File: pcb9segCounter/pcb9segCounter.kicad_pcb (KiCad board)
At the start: 2 copper layers, 72.2 x 78.5 mm, 52 parts, among them J1 SAO, J2 AVR-ISP-6, U1 ATtiny84A-SS

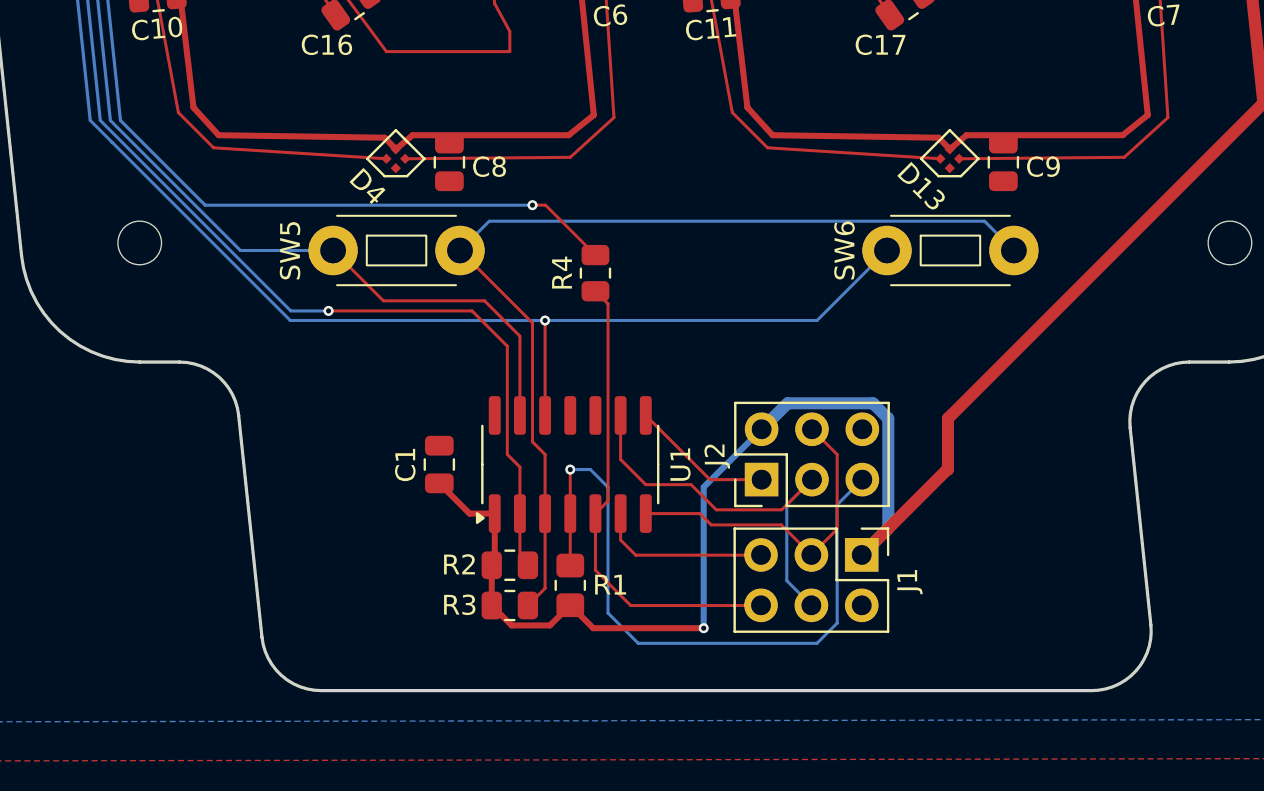
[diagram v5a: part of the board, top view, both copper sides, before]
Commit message: adding 3d model which was used to generate board outline, commiting before adding i2c pullups
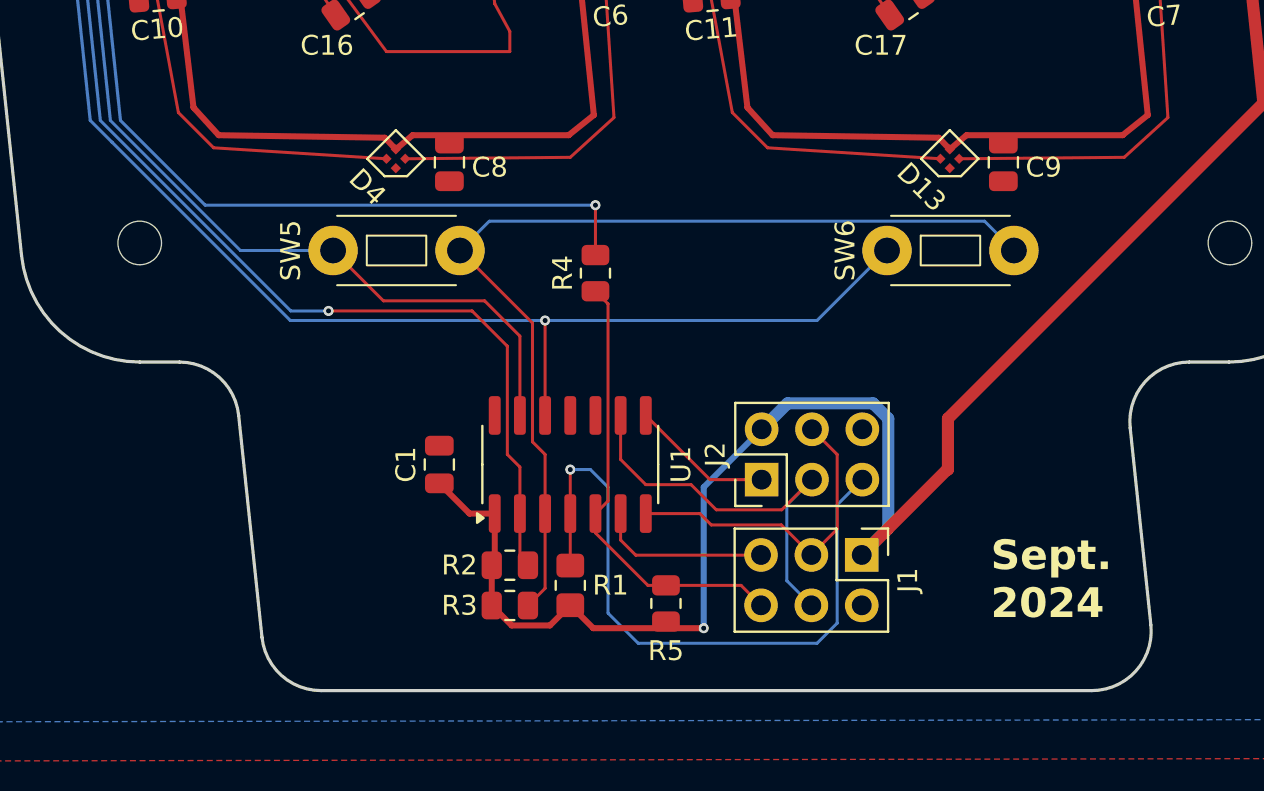
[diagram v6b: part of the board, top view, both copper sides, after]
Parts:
- added R5: 1k, Resistor_SMD:R_0805_2012Metric, F.Cu at (93.0, 113.2)
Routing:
- net /pcb9SegDigit/DIN: track 41.9 -> 43.3 mm
- net GP2: track 23.7 -> 22.6 mm
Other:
- board text added: "Sept. 2024"
- board text added: "github.com/ martinbros/ 9SegCounter"

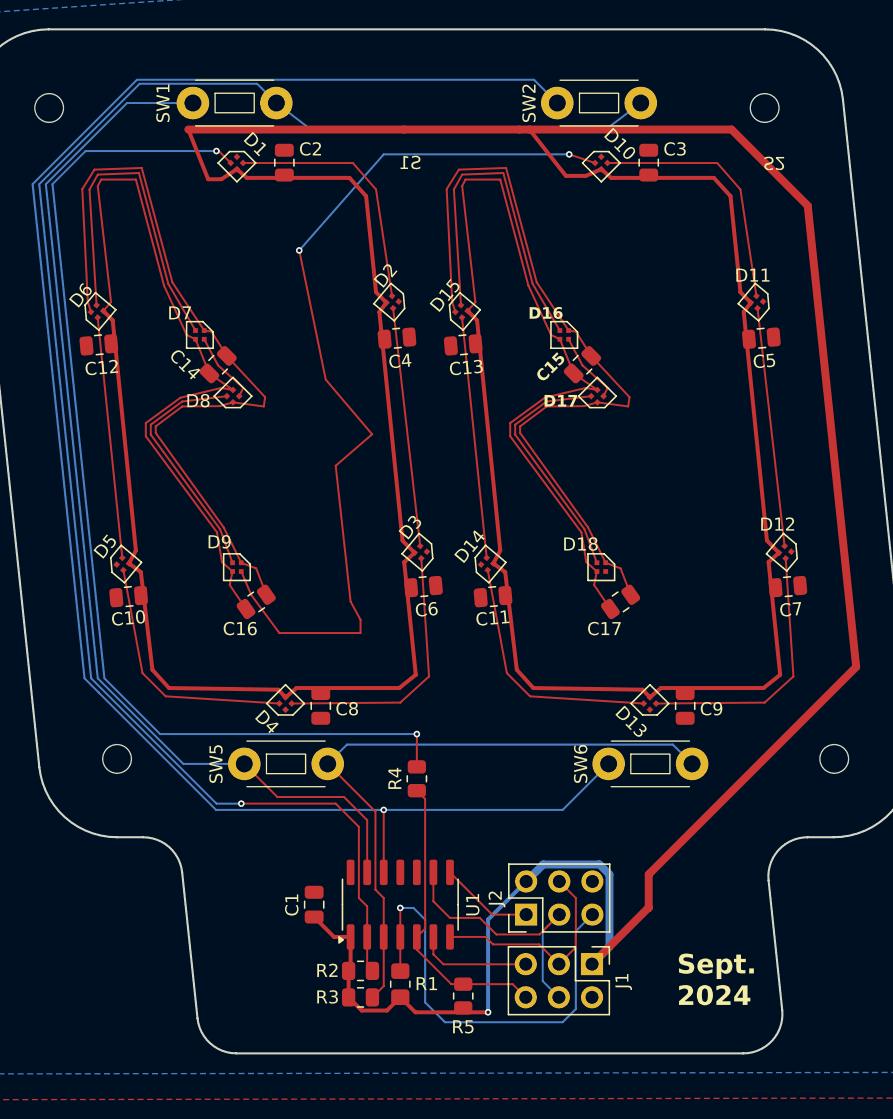
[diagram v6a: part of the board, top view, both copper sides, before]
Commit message: Looks really good, all footprints and implementation check out. Looking to move an LED and adding an additional decap capacitor
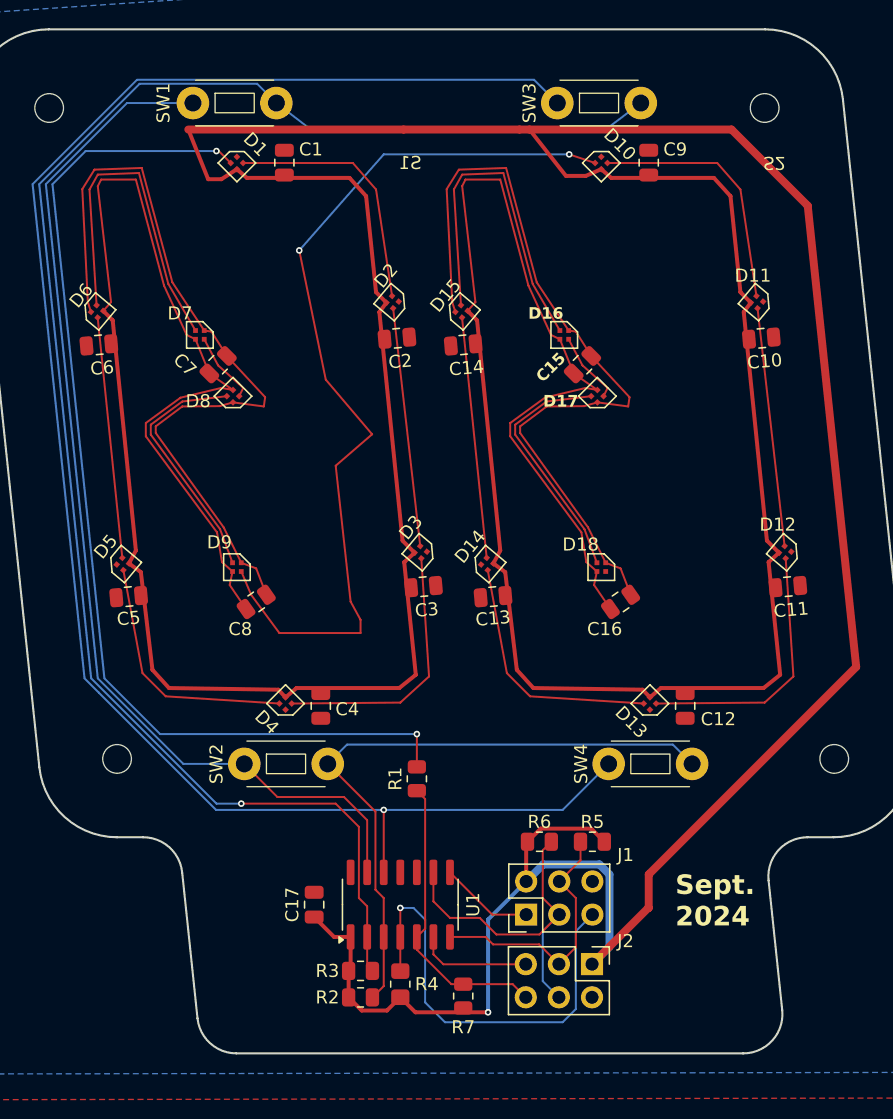
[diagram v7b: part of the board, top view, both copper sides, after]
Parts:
- added R5: 1k, Resistor_SMD:R_0805_2012Metric, F.Cu at (102.9, 101.3)
- added R6: 1k, Resistor_SMD:R_0805_2012Metric, F.Cu at (98.8, 101.3)
- renumbered C2 to C1, C5 to C10, C7 to C11, C9 to C12, C11 to C13, C13 to C14, C17 to C16, C1 to C17, C4 to C2, C6 to C3, C8 to C4, C10 to C5, C12 to C6, C14 to C7, C16 to C8, C3 to C9, J2 to J1, J1 to J2, R4 to R1, R3 to R2, R2 to R3, R1 to R4, R5 to R7, SW5 to SW2, SW2 to SW3, SW6 to SW4
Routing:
- net +5V: track 450.8 -> 460.6 mm
- net SCL: track 20.9 -> 27.3 mm
- net SDA: track 16.6 -> 20.3 mm

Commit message: Everything looks good for manufacture
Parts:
- added C17: 0.1u, Capacitor_SMD:C_0805_2012Metric, F.Cu at (100.7, 66.7)
- added C8: 0.1u, Capacitor_SMD:C_0805_2012Metric, F.Cu at (72.8, 66.7)
- moved C7 7.84 mm to (77.1, 57.5)
- moved C16 7.84 mm to (105.1, 57.5)
- moved D7 6.57 mm to (78.9, 60.1)
- moved D16 6.57 mm to (106.8, 60.1)
- moved D8 0.15 mm to (75.4, 67.3)
- moved D17 0.15 mm to (103.4, 67.3)
- renumbered C9 to C10, C10 to C11, C11 to C12, C12 to C13, C13 to C14, C14 to C15, C15 to C16, C16 to C18, C17 to C19, C8 to C9
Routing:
- net /pcb9SegDigit/DOUT: track 70.3 -> 37.5 mm
- net +5V: track 460.6 -> 491.8 mm
- net GND: track 121.7 -> 145.7 mm
- net Net-(D16-DOUT): track 5.56 -> 15.8 mm
- net Net-(D7-DOUT): track 5.56 -> 15.8 mm
- net Net-(D6-DOUT): track 26.3 -> 29.7 mm
- net Net-(D15-DOUT): track 26.3 -> 29.7 mm
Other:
- board text added: "5V"
- board text added: "G1"
- board text added: "G2"
- board text added: "GND"
- board text added: "MISO"
- board text added: "RST"
- board text added: "SAO"
